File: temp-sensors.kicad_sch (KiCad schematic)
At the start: 40 parts, among them U38 TMP75AIDR, U39 TMP75AIDR, U40 TMP75AIDR, U42 NTS0104_DHVQFN

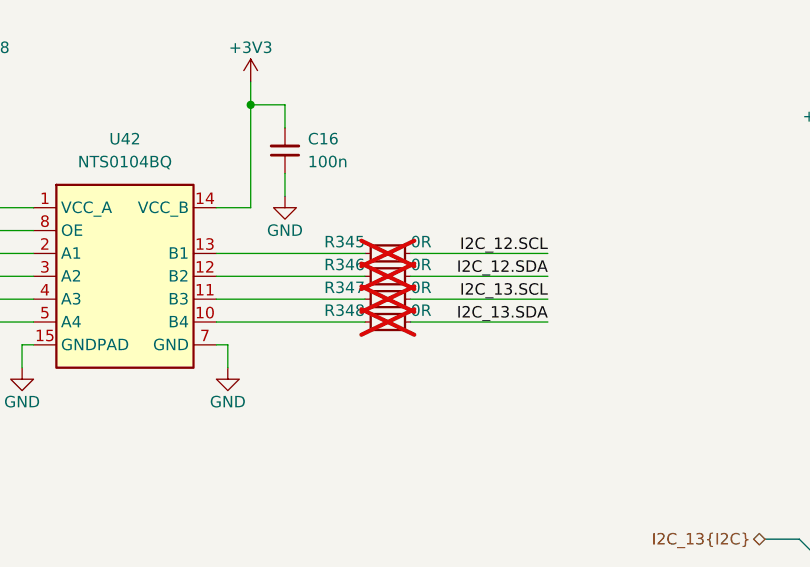
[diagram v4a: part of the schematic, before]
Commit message: [#83767] Add more I2C connections
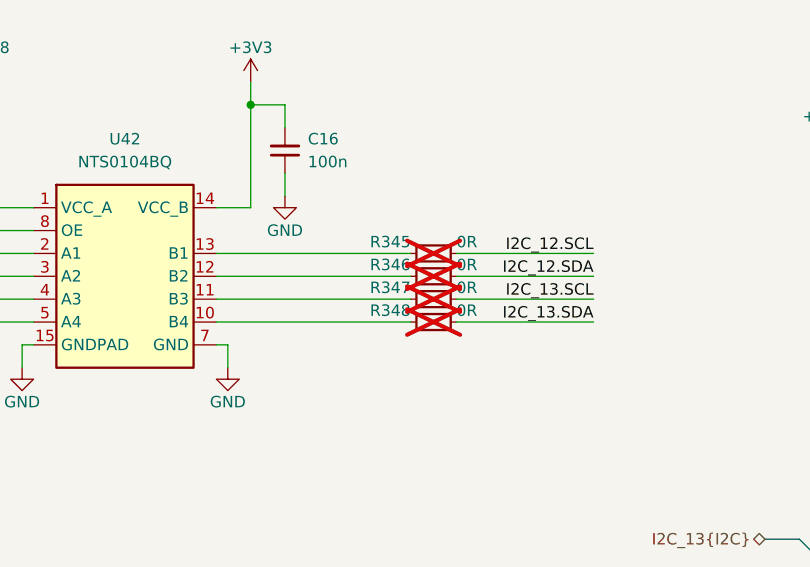
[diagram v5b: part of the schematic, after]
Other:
- moved on the sheet: R345, R346, R347, R348
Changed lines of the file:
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@@
 	(wire
 		(pts
-			(xy 149.86 167.64) (xy 134.62 167.64)
+			(xy 154.94 167.64) (xy 139.7 167.64)
 		)
 		(stroke
@@
 	(wire
 		(pts
-			(xy 149.86 165.1) (xy 134.62 165.1)
+			(xy 154.94 165.1) (xy 139.7 165.1)
 		)
 		(stroke
@@
 	(wire
 		(pts
-			(xy 113.03 162.56) (xy 129.54 162.56)
+			(xy 113.03 162.56) (xy 134.62 162.56)
 		)
 		(stroke
@@
 	(wire
 		(pts
-			(xy 149.86 162.56) (xy 134.62 162.56)
+			(xy 154.94 162.56) (xy 139.7 162.56)
 		)
 		(stroke
@@
 	(wire
 		(pts
-			(xy 113.03 165.1) (xy 129.54 165.1)
+			(xy 113.03 165.1) (xy 134.62 165.1)
 		)
 		(stroke
@@
 	(wire
 		(pts
-			(xy 149.86 170.18) (xy 134.62 170.18)
+			(xy 154.94 170.18) (xy 139.7 170.18)
 		)
 		(stroke
@@
 	(wire
 		(pts
-			(xy 113.03 170.18) (xy 129.54 170.18)
+			(xy 113.03 170.18) (xy 134.62 170.18)
 		)
 		(stroke
@@
 	(wire
 		(pts
-			(xy 113.03 167.64) (xy 129.54 167.64)
+			(xy 113.03 167.64) (xy 134.62 167.64)
 		)
 		(stroke
@@
 	)
 	(label "I2C_13.SCL"
-		(at 149.86 167.64 180)
+		(at 154.94 167.64 180)
 		(effects
 			(font
@@
 	)
 	(label "I2C_12.SDA"
-		(at 149.86 165.1 180)
+		(at 154.94 165.1 180)
 		(effects
 			(font
@@
 	)
 	(label "I2C_13.SDA"
-		(at 149.86 170.18 180)
+		(at 154.94 170.18 180)
 		(effects
 			(font
@@
 	)
 	(label "I2C_12.SCL"
-		(at 149.86 162.56 180)
+		(at 154.94 162.56 180)
 		(effects
 			(font
@@
 	(symbol
 		(lib_id "antmicroResistors0402:R_0R_0402")
-		(at 129.54 167.64 0)
+		(at 134.62 167.64 0)
 		(unit 1)
 		(exclude_from_sim no)
@@
 		(dnp yes)
 		(property "Reference" "R347"
-			(at 129.54 166.37 0)
+			(at 134.62 166.37 0)
 			(effects
 				(font
@@
 		)
 		(property "Value" "R_0R_0402"
-			(at 149.86 180.34 0)
+			(at 154.94 180.34 0)
 			(effects
 				(font
@@
 		)
 		(property "Footprint" "antmicro-footprints:R_0402_1005Metric"
-			(at 149.86 182.88 0)
+			(at 154.94 182.88 0)
 			(effects
 				(font
@@
 		)
 		(property "Datasheet" "https://industrial.panasonic.com/cdbs/www-data/pdf/RDA0000/AOA0000C301.pdf"
-			(at 149.86 185.42 0)
+			(at 154.94 185.42 0)
 			(effects
 				(font
@@
 		)
 		(property "Description" "SMD Chip Resistor, Jumper, 0 ohm, 100 mW, 0402 [1005 Metric], Thick Film, General Purpose"
-			(at 129.54 167.64 0)
+			(at 134.62 167.64 0)
 			(effects
 				(font
@@
 		)
 		(property "MPN" "ERJ2GE0R00X"
-			(at 149.86 187.96 0)
+			(at 154.94 187.96 0)
 			(effects
 				(font
@@
 		)
 		(property "Manufacturer" "Panasonic"
-			(at 149.86 190.5 0)
+			(at 154.94 190.5 0)
 			(effects
 				(font
@@
 		)
 		(property "License" "Apache-2.0"
-			(at 149.86 193.04 0)
+			(at 154.94 193.04 0)
 			(effects
 				(font
@@
 		)
 		(property "Author" "Antmicro"
-			(at 149.86 195.58 0)
+			(at 154.94 195.58 0)
 			(effects
 				(font
@@
 		)
 		(property "Val" "0R"
-			(at 134.62 166.37 0)
+			(at 139.7 166.37 0)
 			(effects
 				(font
@@
 		)
 		(property "Tolerance" "~"
-			(at 149.86 177.8 0)
+			(at 154.94 177.8 0)
 			(effects
 				(font
@@
 		)
 		(property "Current" "1A"
-			(at 149.86 198.12 0)
+			(at 154.94 198.12 0)
 			(effects
 				(font
@@
 	(symbol
 		(lib_id "antmicroResistors0402:R_0R_0402")
-		(at 129.54 170.18 0)
+		(at 134.62 170.18 0)
 		(unit 1)
 		(exclude_from_sim no)
@@
 		(dnp yes)
 		(property "Reference" "R348"
-			(at 129.54 168.91 0)
+			(at 134.62 168.91 0)
 			(effects
 				(font
@@
 		)
 		(property "Value" "R_0R_0402"
-			(at 149.86 182.88 0)
+			(at 154.94 182.88 0)
 			(effects
 				(font
@@
 		)
 		(property "Footprint" "antmicro-footprints:R_0402_1005Metric"
-			(at 149.86 185.42 0)
+			(at 154.94 185.42 0)
 			(effects
 				(font
@@
 		)
 		(property "Datasheet" "https://industrial.panasonic.com/cdbs/www-data/pdf/RDA0000/AOA0000C301.pdf"
-			(at 149.86 187.96 0)
+			(at 154.94 187.96 0)
 			(effects
 				(font
@@
 		)
 		(property "Description" "SMD Chip Resistor, Jumper, 0 ohm, 100 mW, 0402 [1005 Metric], Thick Film, General Purpose"
-			(at 129.54 170.18 0)
+			(at 134.62 170.18 0)
 			(effects
 				(font
@@
 		)
 		(property "MPN" "ERJ2GE0R00X"
-			(at 149.86 190.5 0)
+			(at 154.94 190.5 0)
 			(effects
 				(font
@@
 		)
 		(property "Manufacturer" "Panasonic"
-			(at 149.86 193.04 0)
+			(at 154.94 193.04 0)
 			(effects
 				(font
@@
 		)
 		(property "License" "Apache-2.0"
-			(at 149.86 195.58 0)
+			(at 154.94 195.58 0)
 			(effects
 				(font
@@
 		)
 		(property "Author" "Antmicro"
-			(at 149.86 198.12 0)
+			(at 154.94 198.12 0)
 			(effects
 				(font
@@
 		)
 		(property "Val" "0R"
-			(at 134.62 168.91 0)
+			(at 139.7 168.91 0)
 			(effects
 				(font
@@
 		)
 		(property "Tolerance" "~"
-			(at 149.86 180.34 0)
+			(at 154.94 180.34 0)
 			(effects
 				(font
@@
 		)
 		(property "Current" "1A"
-			(at 149.86 200.66 0)
+			(at 154.94 200.66 0)
 			(effects
 				(font
@@
 	(symbol
 		(lib_id "antmicroResistors0402:R_0R_0402")
-		(at 129.54 162.56 0)
+		(at 134.62 162.56 0)
 		(unit 1)
 		(exclude_from_sim no)
@@
 		(dnp yes)
 		(property "Reference" "R345"
-			(at 129.54 161.29 0)
+			(at 134.62 161.29 0)
 			(effects
 				(font
@@
 		)
 		(property "Value" "R_0R_0402"
-			(at 149.86 175.26 0)
+			(at 154.94 175.26 0)
 			(effects
 				(font
@@
 		)
 		(property "Footprint" "antmicro-footprints:R_0402_1005Metric"
-			(at 149.86 177.8 0)
+			(at 154.94 177.8 0)
 			(effects
 				(font
@@
 		)
 		(property "Datasheet" "https://industrial.panasonic.com/cdbs/www-data/pdf/RDA0000/AOA0000C301.pdf"
-			(at 149.86 180.34 0)
+			(at 154.94 180.34 0)
 			(effects
 				(font
@@
 		)
 		(property "Description" "SMD Chip Resistor, Jumper, 0 ohm, 100 mW, 0402 [1005 Metric], Thick Film, General Purpose"
-			(at 129.54 162.56 0)
+			(at 134.62 162.56 0)
 			(effects
 				(font
@@
 		)
 		(property "MPN" "ERJ2GE0R00X"
-			(at 149.86 182.88 0)
+			(at 154.94 182.88 0)
 			(effects
 				(font
@@
 		)
 		(property "Manufacturer" "Panasonic"
-			(at 149.86 185.42 0)
+			(at 154.94 185.42 0)
 			(effects
 				(font
@@
 		)
 		(property "License" "Apache-2.0"
-			(at 149.86 187.96 0)
+			(at 154.94 187.96 0)
 			(effects
 				(font
@@
 		)
 		(property "Author" "Antmicro"
-			(at 149.86 190.5 0)
+			(at 154.94 190.5 0)
 			(effects
 				(font
@@
 		)
 		(property "Val" "0R"
-			(at 134.62 161.29 0)
+			(at 139.7 161.29 0)
 			(effects
 				(font
@@
 		)
 		(property "Tolerance" "~"
-			(at 149.86 172.72 0)
+			(at 154.94 172.72 0)
 			(effects
 				(font
@@
 		)
 		(property "Current" "1A"
-			(at 149.86 193.04 0)
+			(at 154.94 193.04 0)
 			(effects
 				(font
@@
 	(symbol
 		(lib_id "antmicroResistors0402:R_0R_0402")
-		(at 129.54 165.1 0)
+		(at 134.62 165.1 0)
 		(unit 1)
 		(exclude_from_sim no)
@@
 		(dnp yes)
 		(property "Reference" "R346"
-			(at 129.54 163.83 0)
+			(at 134.62 163.83 0)
 			(effects
 				(font
@@
 		)
 		(property "Value" "R_0R_0402"
-			(at 149.86 177.8 0)
+			(at 154.94 177.8 0)
 			(effects
 				(font
@@
 		)
 		(property "Footprint" "antmicro-footprints:R_0402_1005Metric"
-			(at 149.86 180.34 0)
+			(at 154.94 180.34 0)
 			(effects
 				(font
@@
 		)
 		(property "Datasheet" "https://industrial.panasonic.com/cdbs/www-data/pdf/RDA0000/AOA0000C301.pdf"
-			(at 149.86 182.88 0)
+			(at 154.94 182.88 0)
 			(effects
 				(font
@@
 		)
 		(property "Description" "SMD Chip Resistor, Jumper, 0 ohm, 100 mW, 0402 [1005 Metric], Thick Film, General Purpose"
-			(at 129.54 165.1 0)
+			(at 134.62 165.1 0)
 			(effects
 				(font
@@
 		)
 		(property "MPN" "ERJ2GE0R00X"
-			(at 149.86 185.42 0)
+			(at 154.94 185.42 0)
 			(effects
 				(font
@@
 		)
 		(property "Manufacturer" "Panasonic"
-			(at 149.86 187.96 0)
+			(at 154.94 187.96 0)
 			(effects
 				(font
@@
 		)
 		(property "License" "Apache-2.0"
-			(at 149.86 190.5 0)
+			(at 154.94 190.5 0)
 			(effects
 				(font
@@
 		)
 		(property "Author" "Antmicro"
-			(at 149.86 193.04 0)
+			(at 154.94 193.04 0)
 			(effects
 				(font
@@
 		)
 		(property "Val" "0R"
-			(at 134.62 163.83 0)
+			(at 139.7 163.83 0)
 			(effects
 				(font
@@
 		)
 		(property "Tolerance" "~"
-			(at 149.86 175.26 0)
+			(at 154.94 175.26 0)
 			(effects
 				(font
@@
 		)
 		(property "Current" "1A"
-			(at 149.86 195.58 0)
+			(at 154.94 195.58 0)
 			(effects
 				(font
